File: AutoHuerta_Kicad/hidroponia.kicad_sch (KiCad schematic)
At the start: 16 parts, among them J1 bornera, K1 RELAY, Q1 BC817, U2 PC817, U3 L7805, U4 FUSIBLE

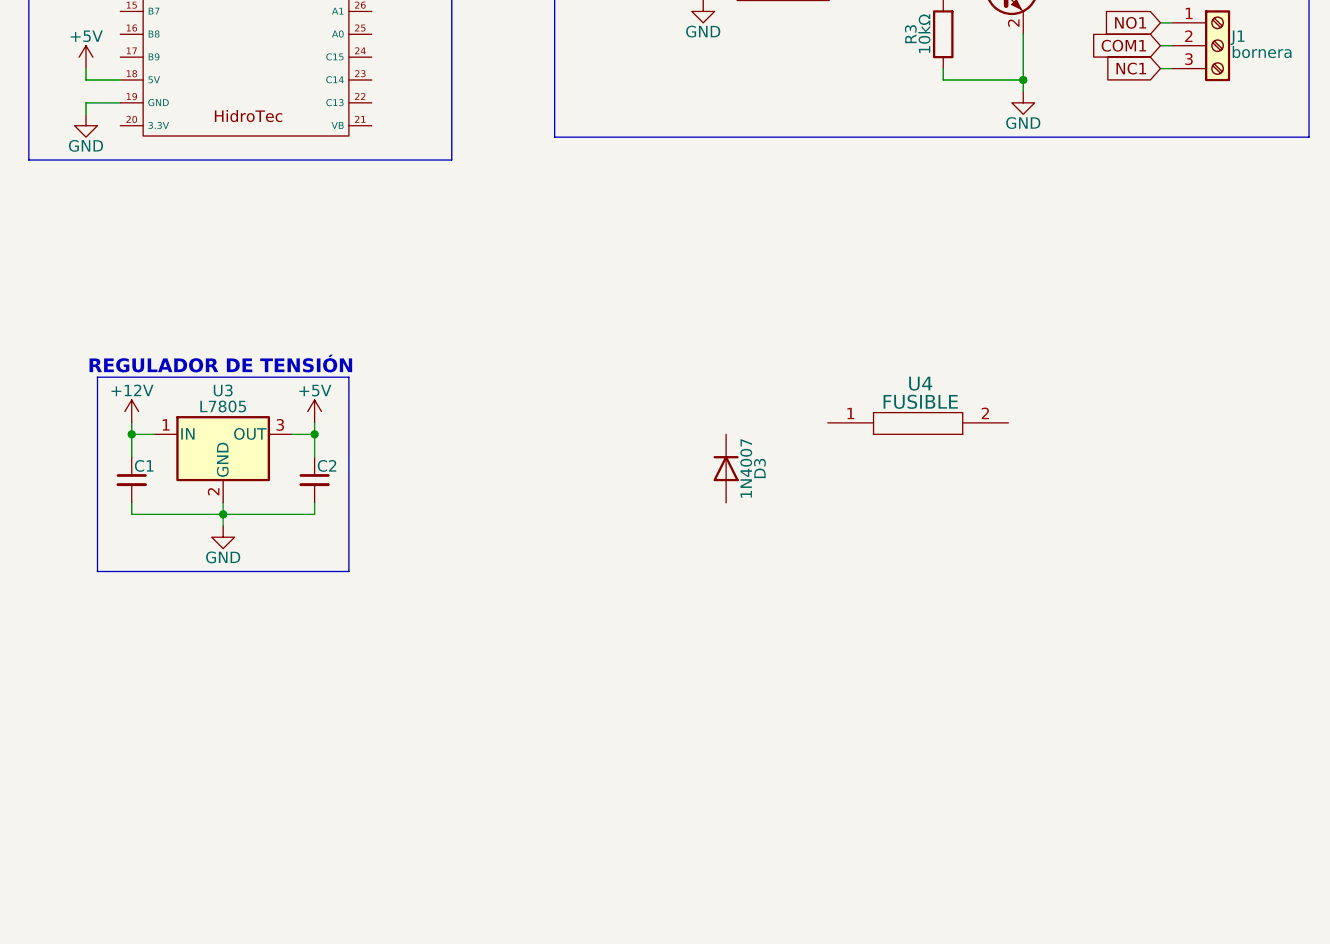
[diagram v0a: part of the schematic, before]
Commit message: Actualizacion de placa
agregamos la entrada de 12v, agregamos el control para el motor, tambien pusimos huellas.
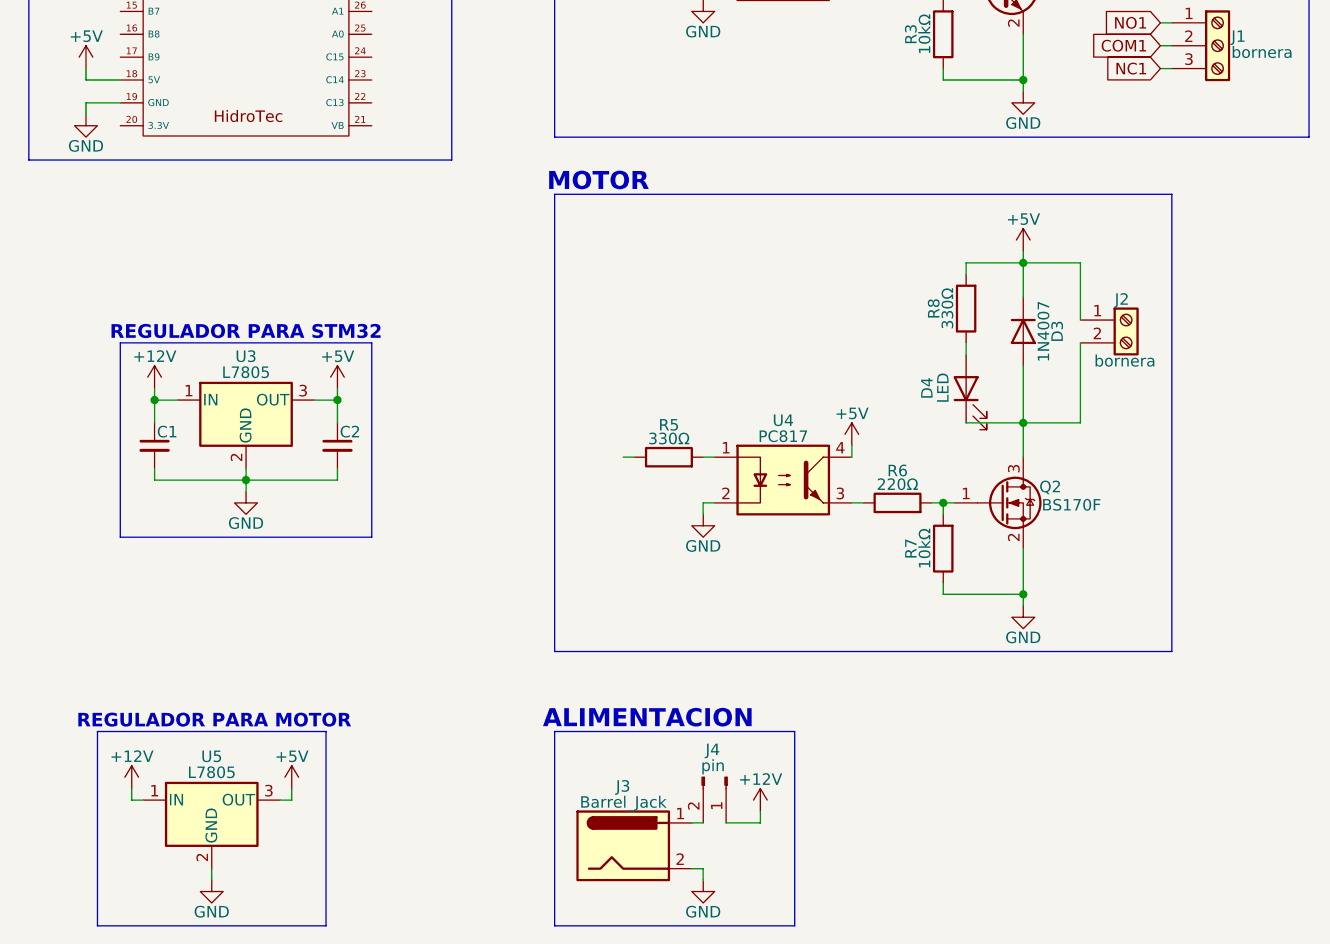
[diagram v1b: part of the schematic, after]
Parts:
- removed U4: FUSIBLE, symbol EESTN5:FUSIBLE
- added D4: LED, LED_THT:LED_D3.0mm, symbol Device:LED
- added J2: bornera, TerminalBlock_MetzConnect:TerminalBlock_MetzConnect_Type011_RT05502HBWC_1x02_P5.00mm_Horizontal, symbol Connector:Screw_Terminal_01x02
- added J3: Barrel_Jack, Connector_BarrelJack:BarrelJack_GCT_DCJ200-10-A_Horizontal, symbol Connector:Barrel_Jack
- added J4: pin, symbol Connector:Conn_01x02_Pin
- added Q2: BS170F, Package_TO_SOT_SMD:SOT-23, symbol Transistor_FET:BS170F
- added R5, R8: 330Ω, Resistor_SMD:R_0805_2012Metric, symbol Device:R
- added R6: 220Ω, Resistor_SMD:R_0805_2012Metric, symbol Device:R
- added R7: 10kΩ, Resistor_SMD:R_0805_2012Metric, symbol Device:R
- added U4: PC817, Package_SO:SSO-4_6.7x5.1mm_P2.54mm_Clearance8mm, symbol Isolator:PC817
- added U5: L7805, symbol Regulator_Linear:L7805
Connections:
- net +12V: now also J4.1 (Pin_1), U5.1 (IN)
- net +5V: now also D3.1 (K), J2.1 (Pin_1), R8.2, U4.4, U5.3 (OUT)
- net GND: now also J3.2, Q2.2 (S), R7.1, U4.2, U5.2 (GND)
- net at D3.2 (A): now also D4.1 (K), J2.2 (Pin_2), Q2.3 (D)
- new net: R5.2, U4.1
- new net: R6.1, U4.3
- new net: Q2.1 (G), R6.2, R7.2
- new net: D4.2 (A), R8.1
- new net: J3.1, J4.2 (Pin_2)
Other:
- note added: "ALIMENTACION"
- note added: "MOTOR"
- note added: "REGULADOR PARA MOTOR"
- note added: "REGULADOR PARA STM32"
- note removed: "REGULADOR DE TENSIÓN"
- moved on the sheet: C1, C2, D3, U3

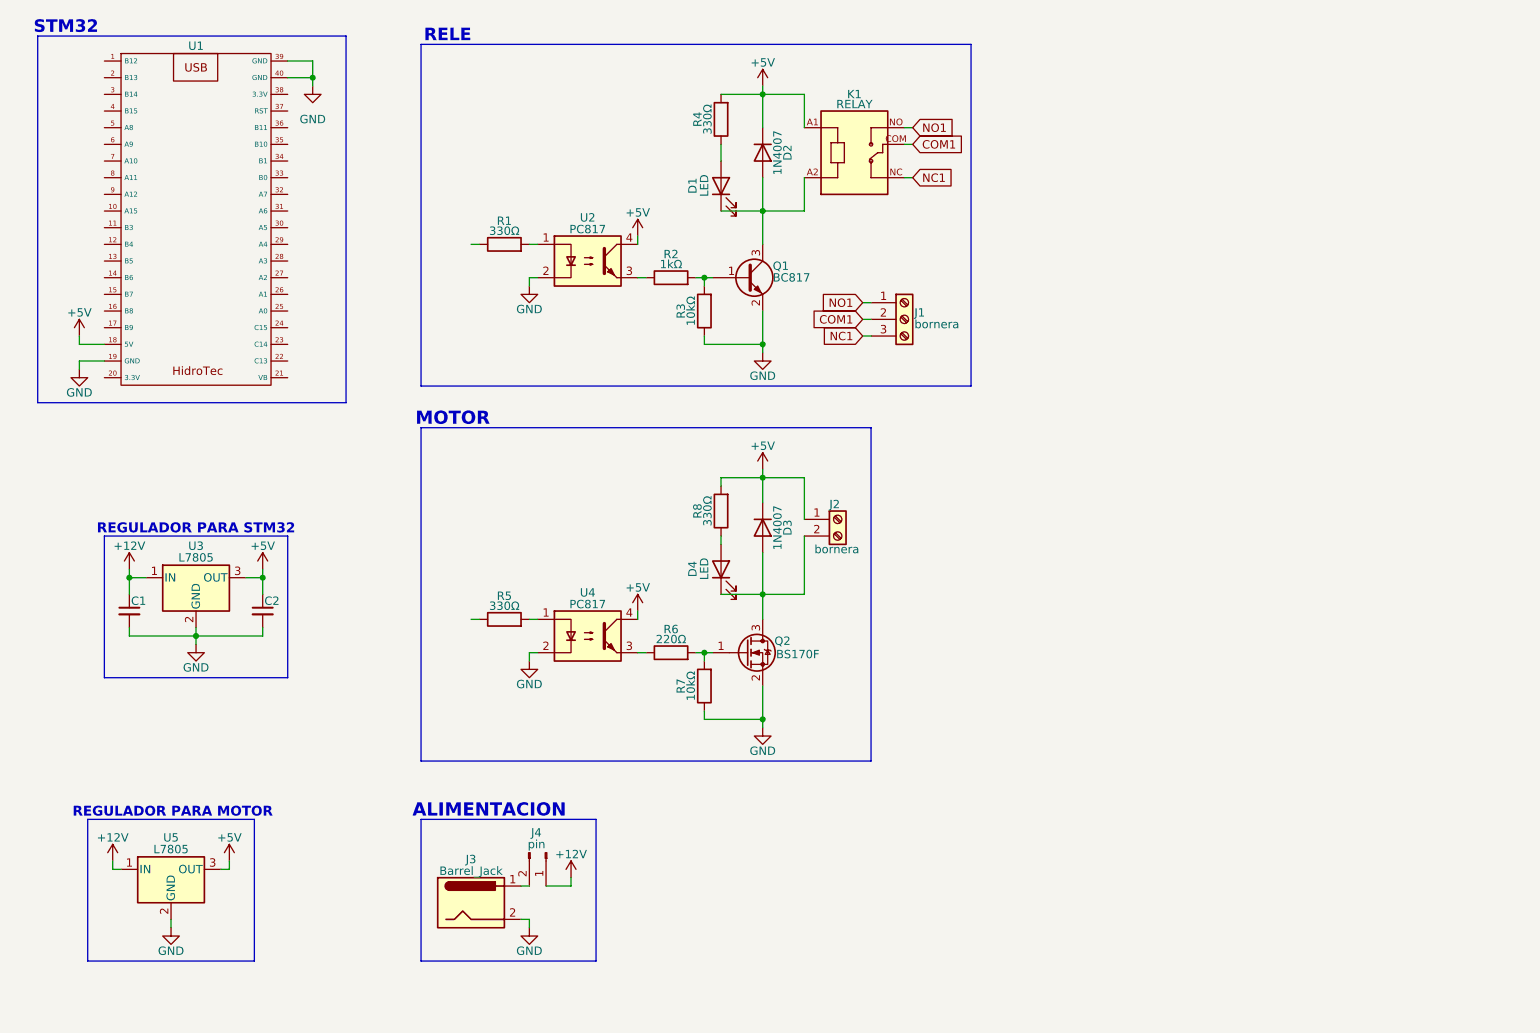
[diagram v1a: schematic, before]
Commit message: Actualizacion de plaqueta 17/4
agregue el control del ventilador, agregue capacito para stm32, puse huellas faltantes y conecte los pines del stm32
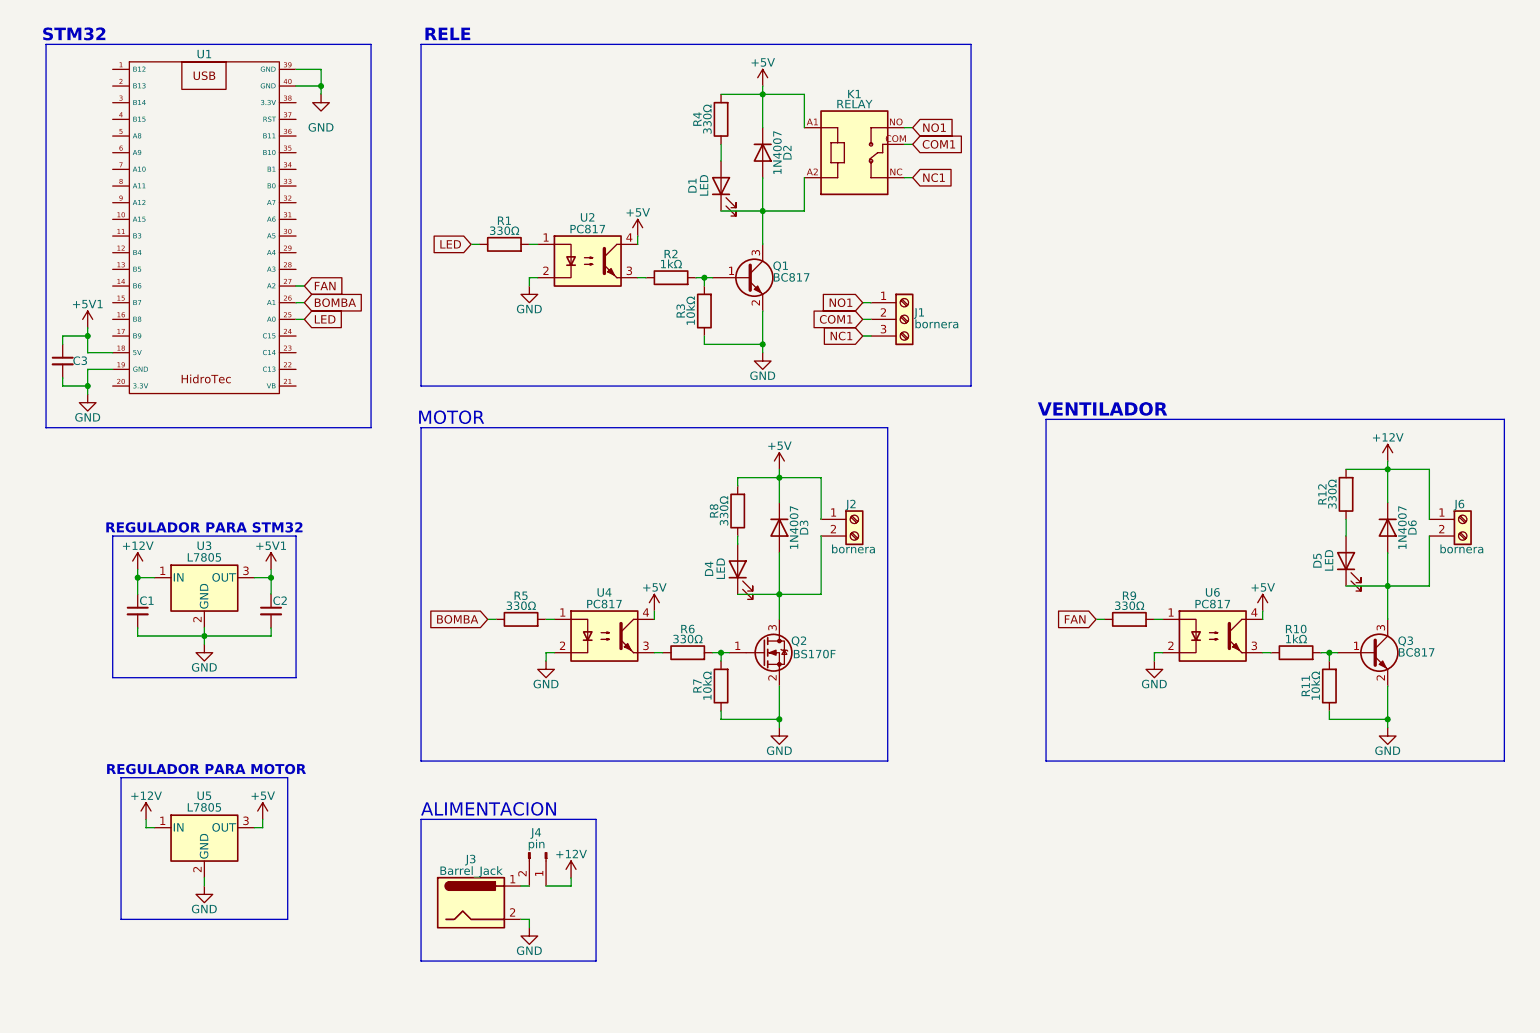
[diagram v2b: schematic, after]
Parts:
- added C3: 0,1uf, Capacitor_SMD:C_0805_2012Metric_Pad1.18x1.45mm_HandSolder, symbol Device:C_Small
- added D5: LED, LED_THT:LED_D3.0mm, symbol Device:LED
- added D6: 1N4007, Diode_SMD:D_SMA, symbol Diode:1N4007
- added J6: bornera, TerminalBlock_MetzConnect:TerminalBlock_MetzConnect_Type011_RT05502HBWC_1x02_P5.00mm_Horizontal, symbol Connector:Screw_Terminal_01x02
- added Q3: BC817, Package_TO_SOT_SMD:SOT-23, symbol Transistor_BJT:BC817
- added R10: 1kΩ, Resistor_SMD:R_0805_2012Metric, symbol Device:R
- added R11: 10kΩ, Resistor_SMD:R_0805_2012Metric, symbol Device:R
- added R12, R9: 330Ω, Resistor_SMD:R_0805_2012Metric, symbol Device:R
- added U6: PC817, Package_SO:SSO-4_6.7x5.1mm_P2.54mm_Clearance8mm, symbol Isolator:PC817
- C1: value C_Small -> 0,33uf; footprint (none) -> Capacitor_SMD:C_0805_2012Metric_Pad1.18x1.45mm_HandSolder
- C2: value C_Small -> 0,1uf; footprint (none) -> Capacitor_SMD:C_0805_2012Metric_Pad1.18x1.45mm_HandSolder
- J4: footprint (none) -> Connector_PinHeader_2.54mm:PinHeader_1x02_P2.54mm_Vertical
- R6: value 220Ω -> 330Ω
- U3, U5: footprint (none) -> Package_TO_SOT_SMD:TO-252-2
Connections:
- net +12V: now also D6.1 (K), J6.1 (Pin_1), R12.2
- net +5V: now also U6.4; no longer C2.1, U1.18 (5V), U3.3 (OUT)
- net GND: now also C3.2, Q3.2 (E), R11.1, U6.2
- net BOMBA: now reaches R5.1
- net BOMBA: now also U1.26 (A1)
- net LED: now reaches R1.1
- net LED: now also U1.25 (A0)
- net FAN: now reaches U1.27 (A2)
- net FAN: now also R9.1
- new net: D5.2 (A), R12.1
- new net: Q3.1 (B), R10.2, R11.2
- new net: D5.1 (K), D6.2 (A), J6.2 (Pin_2), Q3.3 (C)
- new net: R9.2, U6.1
- new net: R10.1, U6.3
- new net +5V1: C2.1, C3.1, U1.18 (5V), U3.3 (OUT)
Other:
- note added: "VENTILADOR"
- moved on the sheet: C1, C2, D3, D4, J2, Q2, R5, R6, R7, R8, U1, U3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

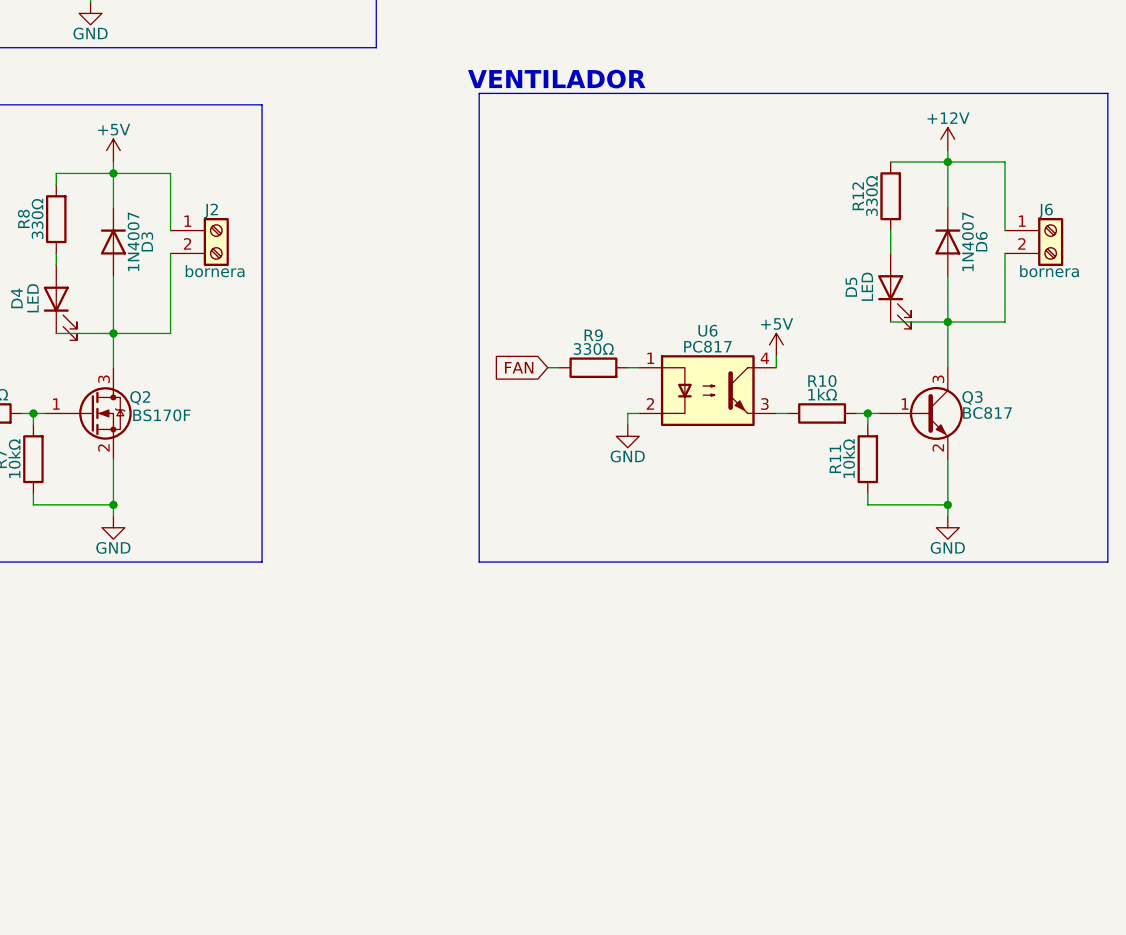
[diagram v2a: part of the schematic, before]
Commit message: Actualizacion de placa
Agregamos pinera de 8 pines y tambien agregamos control de velocidad para el ventilador.
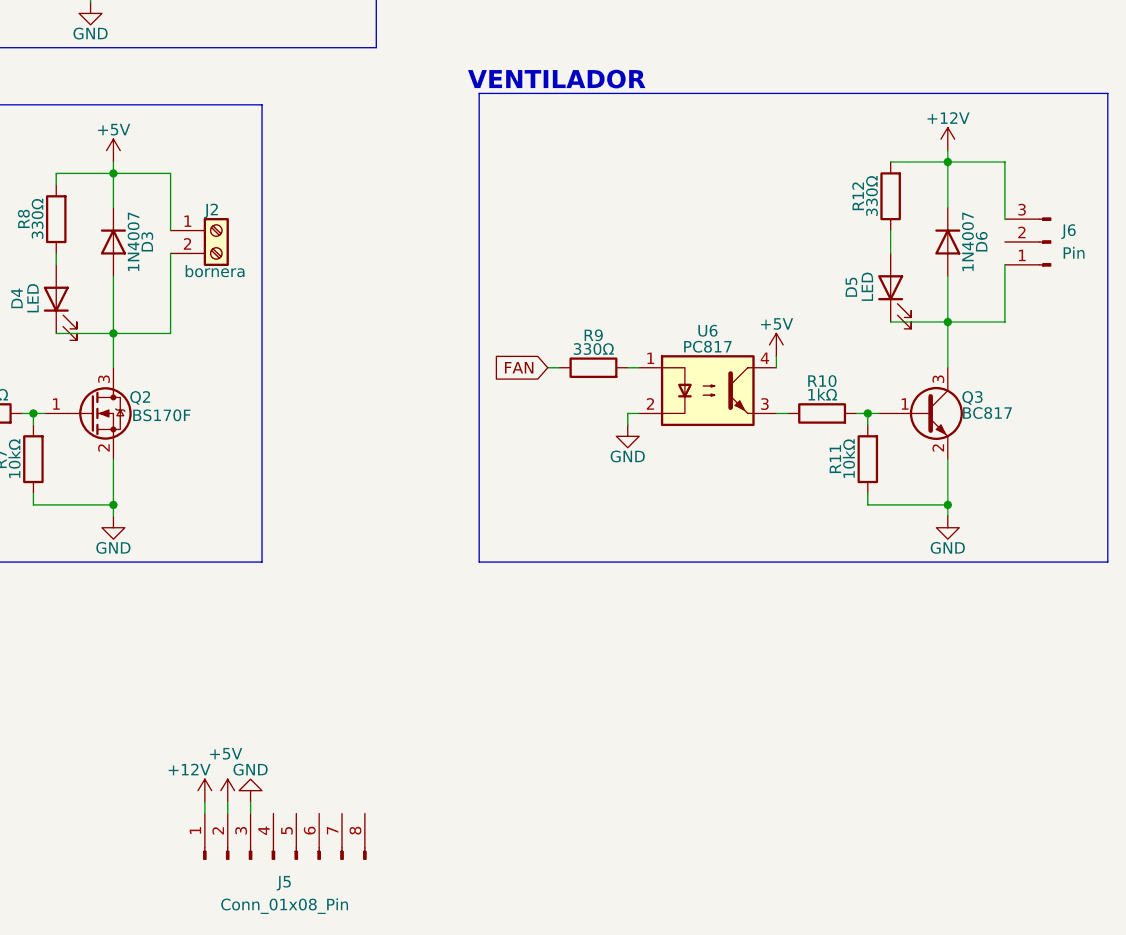
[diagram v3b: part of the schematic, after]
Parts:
- removed J6: bornera, TerminalBlock_MetzConnect:TerminalBlock_MetzConnect_Type011_RT05502HBWC_1x02_P5.00mm_Horizontal, symbol Connector:Screw_Terminal_01x02
- added J5: Conn_01x08_Pin, symbol Connector:Conn_01x08_Pin
- added J6: Pin, Connector_Molex:Molex_KK-254_AE-6410-03A_1x03_P2.54mm_Vertical, symbol Connector:Conn_01x03_Pin
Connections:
- net +12V: now also J5.1 (Pin_1), J6.3 (Pin_3)
- net +5V: now also J5.2 (Pin_2)
- net GND: now also J5.3 (Pin_3)
- net at D5.1 (K), D6.2 (A), Q3.3 (C): now also J6.1 (Pin_1)
